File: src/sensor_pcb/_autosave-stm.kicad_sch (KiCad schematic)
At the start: 1 part, among them U3 STM32L451CET6

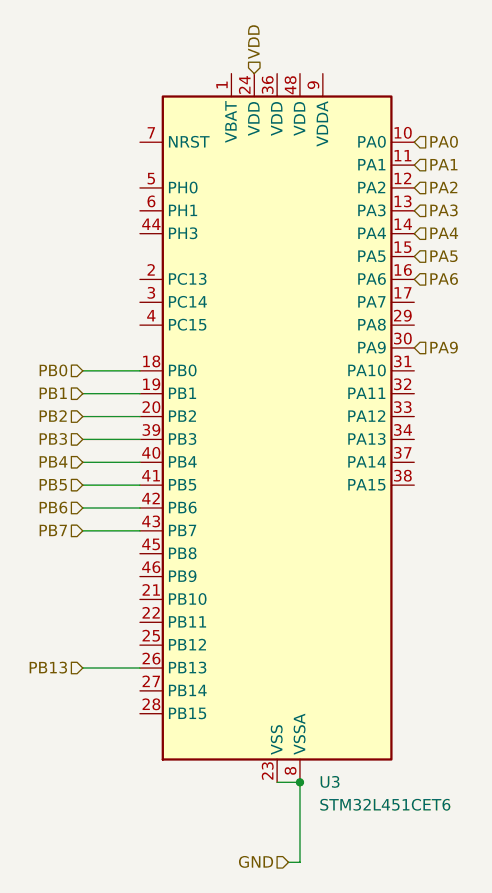
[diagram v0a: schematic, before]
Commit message: fixing up parts according to kicad auto errors
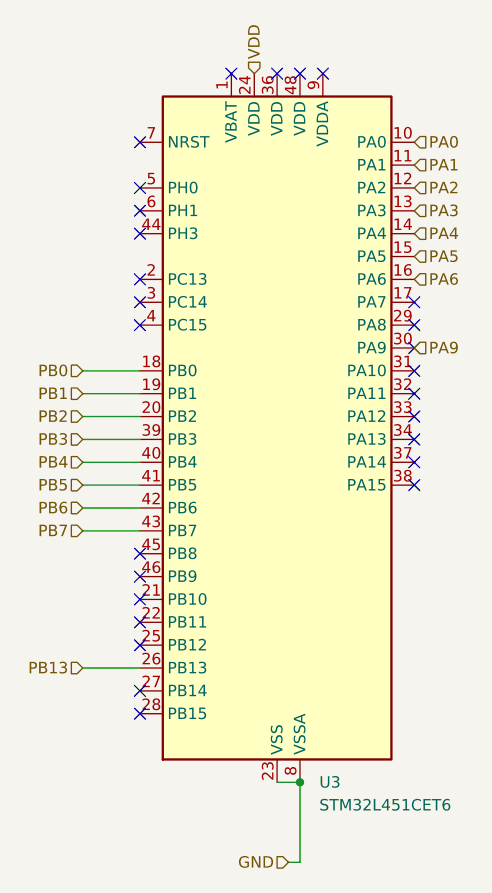
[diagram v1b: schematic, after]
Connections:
- no-connect marks 0 -> 27
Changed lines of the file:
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@@
 		(color 0 0 0 0)
+	)
+	(no_connect
+		(at 54.61 109.22)
+	)
+	(no_connect
+		(at 54.61 106.68)
+	)
+	(no_connect
+		(at 54.61 114.3)
+	)
+	(no_connect
+		(at 54.61 81.28)
+	)
+	(no_connect
+		(at 54.61 124.46)
+	)
+	(no_connect
+		(at 54.61 116.84)
+	)
+	(no_connect
+		(at 85.09 99.06)
+	)
+	(no_connect
+		(at 54.61 111.76)
+	)
+	(no_connect
+		(at 85.09 91.44)
+	)
+	(no_connect
+		(at 54.61 121.92)
+	)
+	(no_connect
+		(at 85.09 96.52)
+	)
+	(no_connect
+		(at 54.61 76.2)
+	)
+	(no_connect
+		(at 64.77 53.34)
+	)
+	(no_connect
+		(at 54.61 68.58)
+	)
+	(no_connect
+		(at 54.61 78.74)
+	)
+	(no_connect
+		(at 74.93 53.34)
+	)
+	(no_connect
+		(at 54.61 60.96)
+	)
+	(no_connect
+		(at 85.09 88.9)
+	)
+	(no_connect
+		(at 54.61 66.04)
+	)
+	(no_connect
+		(at 85.09 78.74)
+	)
+	(no_connect
+		(at 85.09 81.28)
+	)
+	(no_connect
+		(at 85.09 86.36)
+	)
+	(no_connect
+		(at 85.09 83.82)
+	)
+	(no_connect
+		(at 69.85 53.34)
+	)
+	(no_connect
+		(at 72.39 53.34)
+	)
+	(no_connect
+		(at 85.09 93.98)
+	)
+	(no_connect
+		(at 54.61 71.12)
 	)
 	(wire
